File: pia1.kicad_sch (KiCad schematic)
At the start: 39 parts, among them IC25 LM393P, IC31 74LS02N, IC34 MC14050BCP, IC35 MC6821

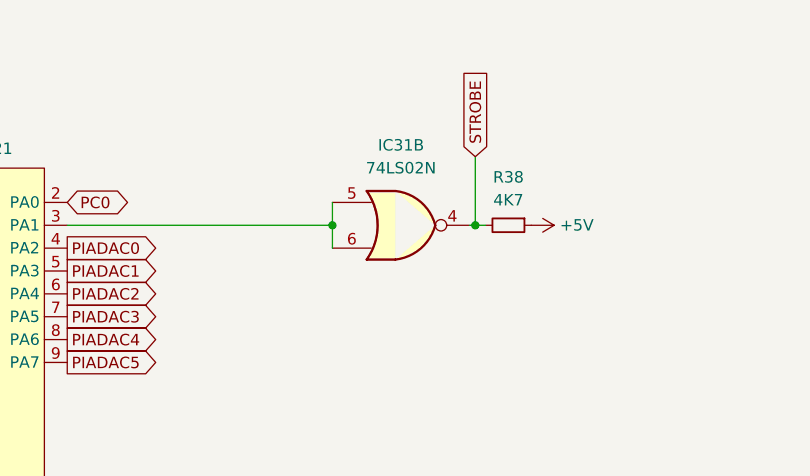
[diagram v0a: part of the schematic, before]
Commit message: add video padding circuit
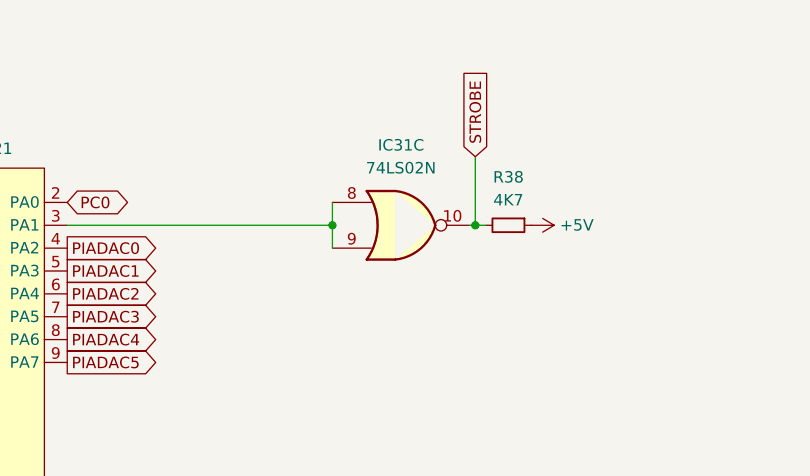
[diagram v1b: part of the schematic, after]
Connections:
- net STROBE: now also IC31.10; no longer IC31.4
- new net: IC31.8, IC31.9, IC35.3 (PA1)
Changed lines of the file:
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@@
 		(lib_id "74xx:74LS02")
 		(at 112.395 41.91 0)
-		(unit 2)
+		(unit 3)
 		(exclude_from_sim no)
 		(in_bom yes)
@@
 				(path "/e3d9e4a2-26cb-4482-98c1-138d9a22d1eb/47fda7cf-0c41-4ecf-b5e2-f0a02b8ccfcb"
 					(reference "IC31")
-					(unit 2)
+					(unit 3)
 				)
 			)

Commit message: FM generator routing
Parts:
- removed RL1: OJS HM FORM A, Dragon:OJS HM 10A Relay, symbol Relay:ADW11
- removed TR1: BC141, Package_TO_SOT_THT:TO-92_Inline_Wide, symbol Transistor_BJT:BC141
- added RL1: OMRON G2E, Dragon:OMRON_G2E, symbol Motorola PIA:G2E
- added TR1: BC141, Package_TO_SOT_THT:TO-92, symbol Device:Q_NPN_ECB
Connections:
- net +12V: now also RL1.5
- net +5V: now also R64.1; no longer R64.2
- net 6bit D/A: now also R64.2; no longer R64.1
- net GND: now also TR1.1 (E)
- net MOTOR: now also R32.2; no longer R32.1
- net MOTOR1: now also RL1.6
- net MOTOR2: now also RL1.4
- net at D1.2 (A): now also RL1.2, TR1.2 (C)
- new net: R32.1, TR1.3 (B)
- no-connect marks 0 -> 2
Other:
- moved on the sheet: C27, D2, D3, IC31C, R32, R38, R64, R72
